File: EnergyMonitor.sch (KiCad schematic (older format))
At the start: 27 parts

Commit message: created symbol for ESP32_D1_MINI
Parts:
- added U?: ESP32_D1_MINI, symbol MyComponents:ESP32_D1_MINI
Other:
- note added: "Current Sensors"
- note added: "Current Transformer\nYHDC SCT-013-00 CT"
- note removed: "CT Current Sensors"

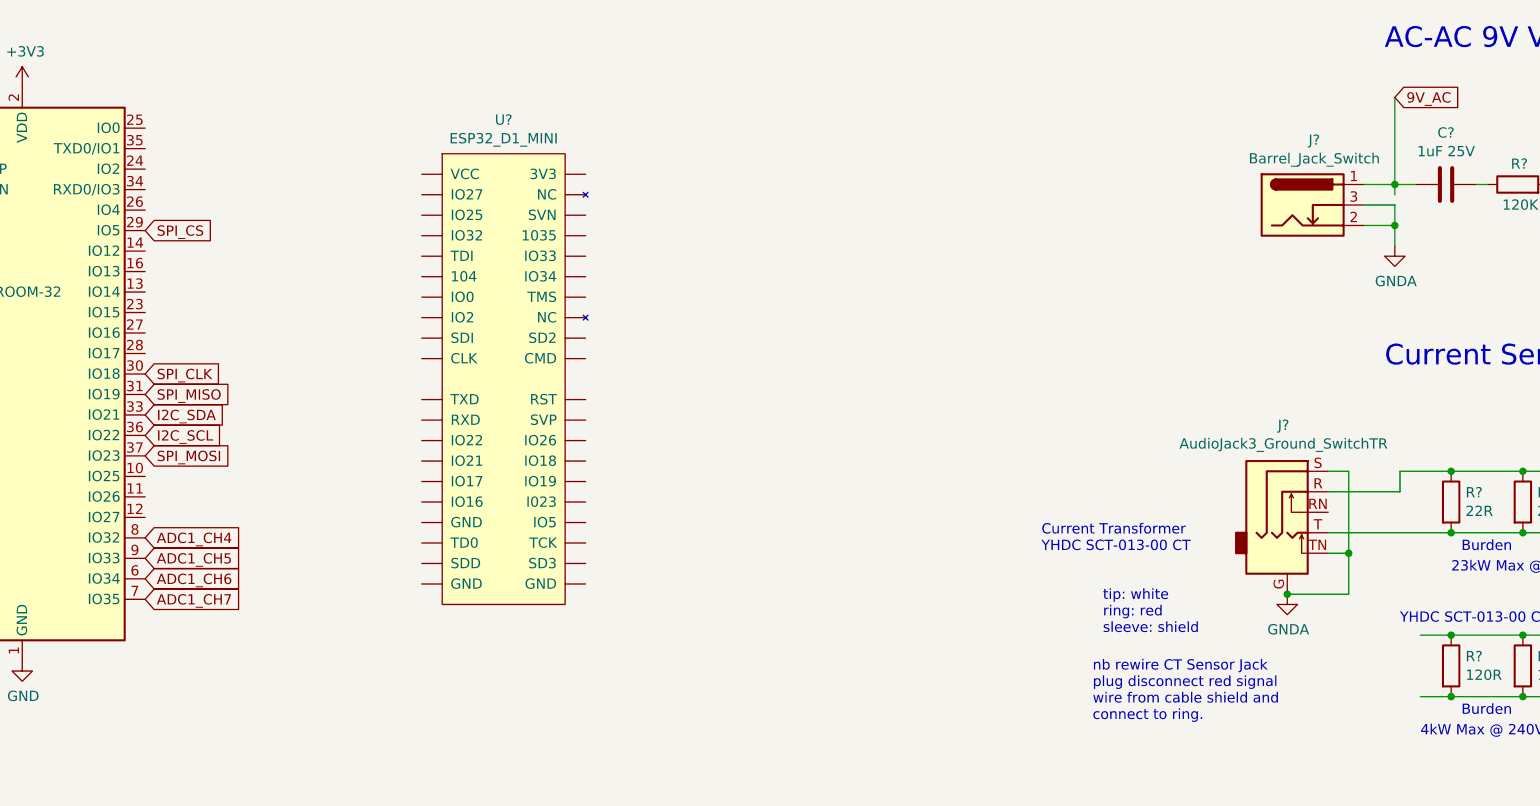
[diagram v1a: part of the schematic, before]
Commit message: edit symbol for ESP32_D1_MINI
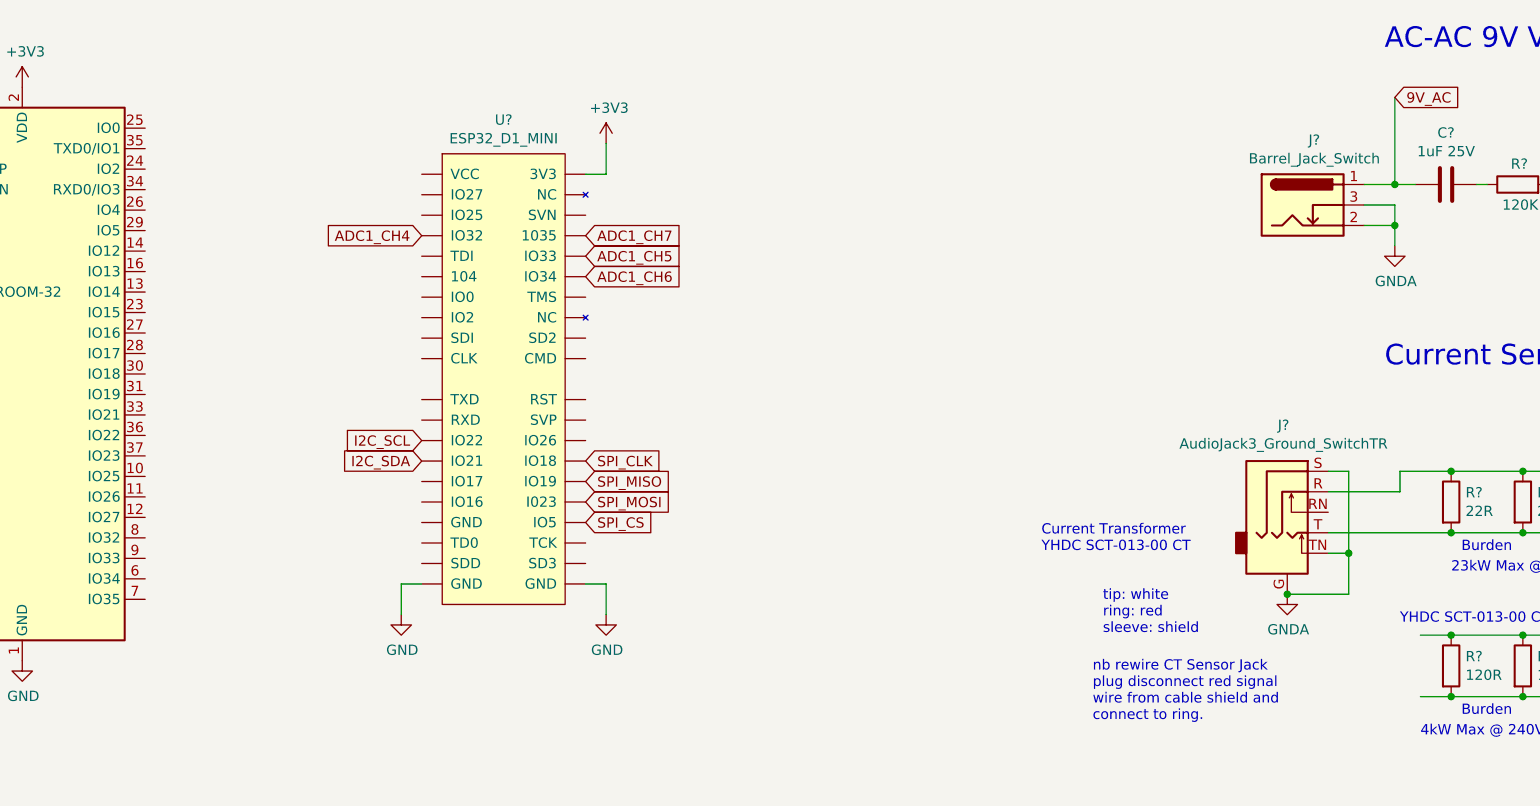
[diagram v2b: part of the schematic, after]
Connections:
- wire segments 47 -> 52
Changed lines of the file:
@@
 Comment4 "klomar"
 $EndDescr
-Text GLabel 2300 3575 2    50   Input ~ 0
+Text GLabel 4450 2100 2    50   Input ~ 0
 ADC1_CH6
-Text GLabel 2300 3675 2    50   Input ~ 0
+Text GLabel 4450 1900 2    50   Input ~ 0
 ADC1_CH7
 $Comp
@@
 Wire Wire Line
 	8800 1650 8850 1650
-Wire Wire Line
-	8400 1700 8400 1650
 Connection ~ 8400 1650
 Wire Wire Line
@@
 Text Notes 3625 7450 0    50   ~ 0
 Remove Jumper\nif ESP32 powered\nby USB.
-Text GLabel 2300 3475 2    50   Input ~ 0
+Text GLabel 4450 2000 2    50   Input ~ 0
 ADC1_CH5
-Text GLabel 2300 3375 2    50   Input ~ 0
+Text GLabel 3650 1900 0    50   Input ~ 0
 ADC1_CH4
-Text GLabel 2300 2875 2    50   Input ~ 0
+Text GLabel 3650 2900 0    50   Input ~ 0
 I2C_SCL
-Text GLabel 2300 2775 2    50   Input ~ 0
+Text GLabel 3650 3000 0    50   Input ~ 0
 I2C_SDA
-Text GLabel 2300 2975 2    50   Input ~ 0
+Text GLabel 4450 3200 2    50   Input ~ 0
 SPI_MOSI
-Text GLabel 2300 2675 2    50   Input ~ 0
+Text GLabel 4450 3100 2    50   Input ~ 0
 SPI_MISO
-Text GLabel 2300 2575 2    50   Input ~ 0
+Text GLabel 4450 3000 2    50   Input ~ 0
 SPI_CLK
-Text GLabel 2300 1875 2    50   Input ~ 0
+Text GLabel 4450 3300 2    50   Input ~ 0
 SPI_CS
 Text GLabel 10475 1100 2    50   Input ~ 0
@@
 	1    0    0    -1
 $EndComp
+$Comp
+L power:GND #PWR?
+U 1 1 613461CB
+P 3550 3750
+F 0 "#PWR?" H 3550 3500 50  0001 C CNN
+F 1 "GND" H 3555 3577 50  0000 C CNN
+F 2 "" H 3550 3750 50  0001 C CNN
+F 3 "" H 3550 3750 50  0001 C CNN
+	1    3550 3750
+	1    0    0    -1
+$EndComp
+$Comp
+L power:GND #PWR?
+U 1 1 61346C95
+P 4550 3750
+F 0 "#PWR?" H 4550 3500 50  0001 C CNN
+F 1 "GND" H 4555 3577 50  0000 C CNN
+F 2 "" H 4550 3750 50  0001 C CNN
+F 3 "" H 4550 3750 50  0001 C CNN
+	1    4550 3750
+	1    0    0    -1
+$EndComp
+Wire Wire Line
+	4450 3600 4550 3600
+Wire Wire Line
+	4550 3600 4550 3750
+Wire Wire Line
+	3650 3600 3550 3600
+Wire Wire Line
+	3550 3600 3550 3750
+$Comp
+L power:+3V3 #PWR?
+U 1 1 6134B5B4
+P 4550 1450
+F 0 "#PWR?" H 4550 1300 50  0001 C CNN
+F 1 "+3V3" H 4565 1623 50  0000 C CNN
+F 2 "" H 4550 1450 50  0001 C CNN
+F 3 "" H 4550 1450 50  0001 C CNN
+	1    4550 1450
+	1    0    0    -1
+$EndComp
+Wire Wire Line
+	4550 1450 4550 1600
+Wire Wire Line
+	4550 1600 4450 1600
 $EndSCHEMATC
